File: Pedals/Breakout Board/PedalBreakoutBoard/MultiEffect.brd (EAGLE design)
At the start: 61.9 x 86.3 mm, 69 parts, among them IC1 LD1117V, IC2 MCP6004P, U1 OPA1652AID

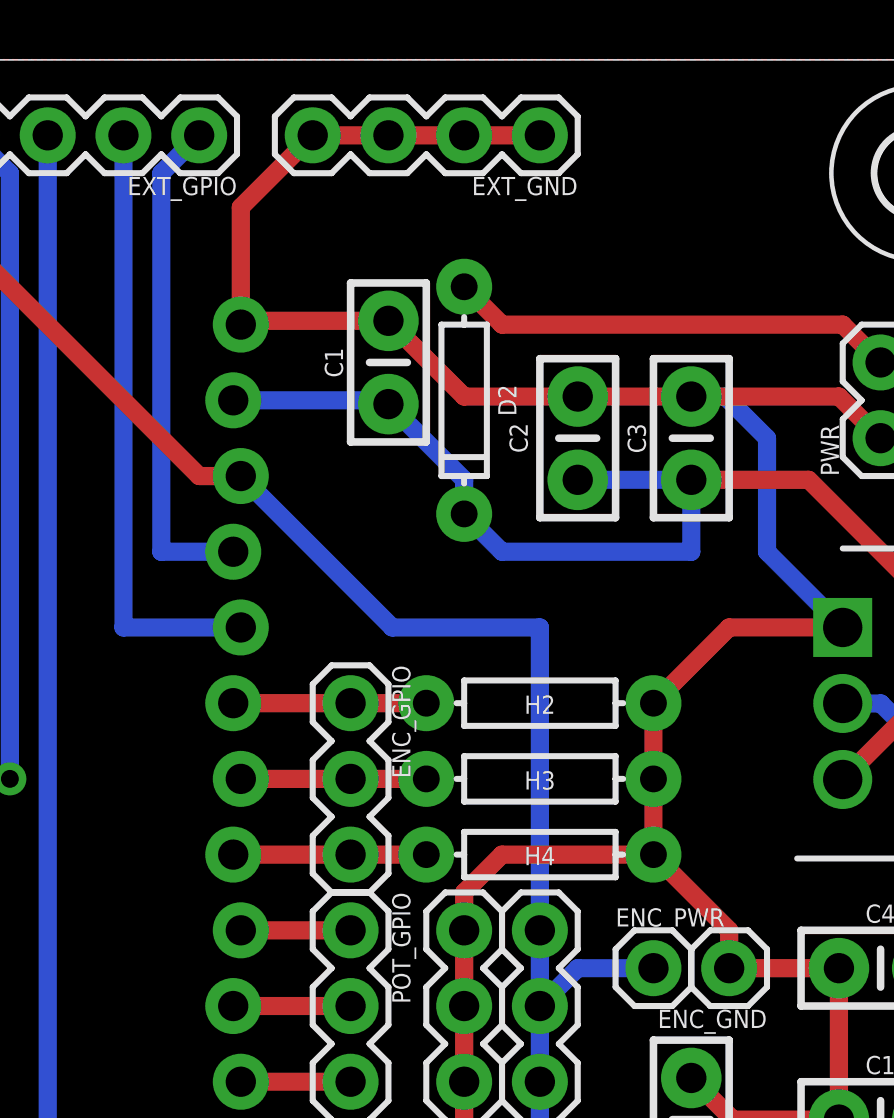
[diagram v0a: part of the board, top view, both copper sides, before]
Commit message: DP-97 - Add power conditioning caps to 3V3_D
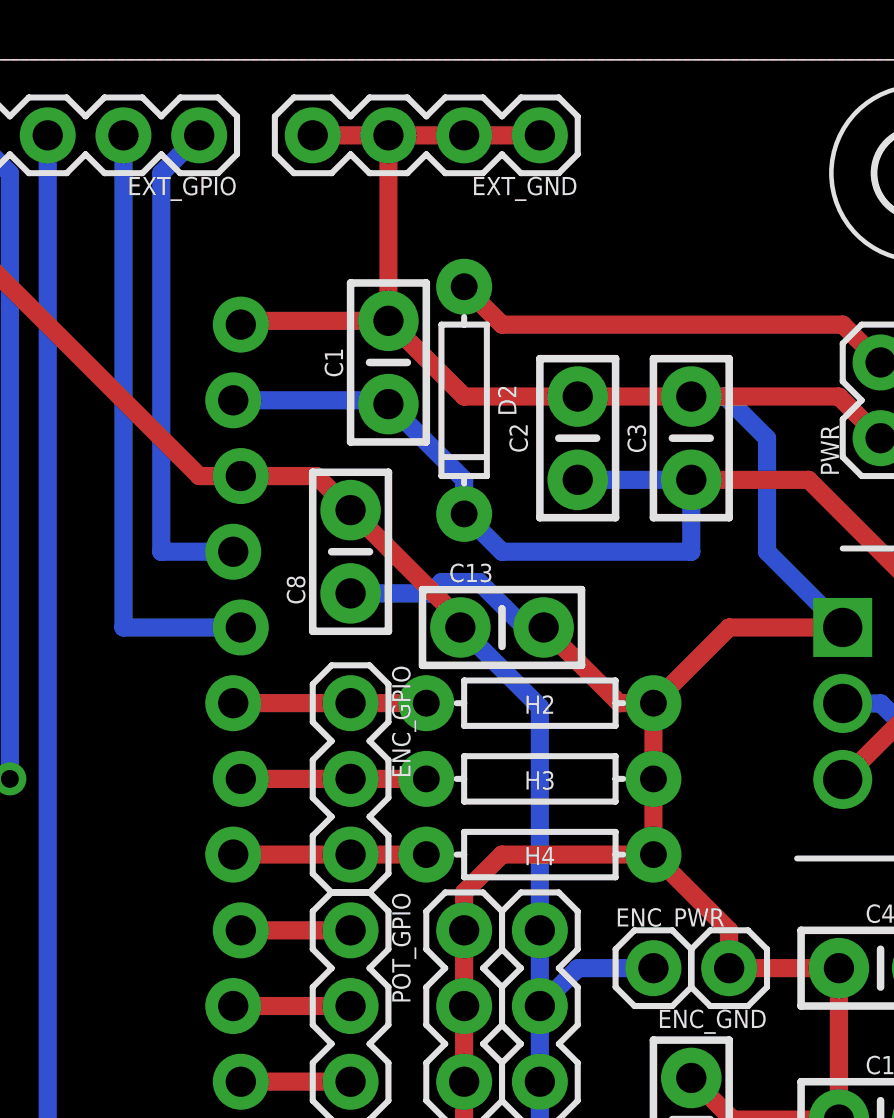
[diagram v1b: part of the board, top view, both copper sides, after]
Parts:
- added C13: 0.1UF, Custom-Parts:CAP-PTH-SMALL-KIT
- added C8: 10UF, Custom-Parts:CAP-PTH-SMALL-KIT
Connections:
- net +3V3_D: now also C13.1, C8.2
- net GND: now also C13.2, C8.1
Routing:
- net GND: track 228.9 -> 239.7 mm
- net +3V3_D: track 132.5 -> 131.1 mm
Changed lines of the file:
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@@
 <attribute name="VALUE" x="17.78" y="85.852" size="0.6096" layer="27" font="vector" ratio="20" rot="R180"/>
+</element>
+<element name="C8" library="Custom-Parts" package="CAP-PTH-SMALL-KIT" value="10UF" x="39.37" y="69.85" smashed="yes" rot="R90">
+<attribute name="NAME" x="37.846" y="68.072" size="0.6096" layer="25" rot="R90"/>
+<attribute name="VALUE" x="41.402" y="68.072" size="0.6096" layer="27" rot="R90"/>
+</element>
+<element name="C13" library="Custom-Parts" package="CAP-PTH-SMALL-KIT" value="0.1UF" x="44.45" y="67.31" smashed="yes">
+<attribute name="NAME" x="42.672" y="68.834" size="0.6096" layer="25"/>
+<attribute name="VALUE" x="42.672" y="65.278" size="0.6096" layer="27"/>
 </element>
 </elements>
 <signals>
 <signal name="GND">
-<contactref element="SEED" pad="40"/>
 <contactref element="PWR" pad="1"/>
 <contactref element="IC1" pad="1"/>
@@
 <contactref element="C1" pad="2"/>
 <wire x1="43.18" y1="75.057" x2="46.99" y2="75.057" width="0.6096" layer="1"/>
-<wire x1="35.687" y1="77.47" x2="35.814" y2="77.597" width="0.6096" layer="1"/>
-<wire x1="35.814" y1="77.597" x2="40.64" y2="77.597" width="0.6096" layer="1"/>
 <wire x1="40.64" y1="77.597" x2="43.18" y2="75.057" width="0.6096" layer="1"/>
 <contactref element="C6" pad="2"/>
@@
 <contactref element="EXT_GND" pad="3"/>
 <contactref element="EXT_GND" pad="4"/>
-<wire x1="35.687" y1="77.47" x2="35.687" y2="81.407" width="0.6096" layer="1"/>
-<wire x1="35.687" y1="81.407" x2="38.1" y2="83.82" width="0.6096" layer="1"/>
 <wire x1="38.1" y1="83.82" x2="40.64" y2="83.82" width="0.6096" layer="1"/>
 <wire x1="40.64" y1="83.82" x2="43.18" y2="83.82" width="0.6096" layer="1"/>
@@
 <wire x1="19.4155" y1="27.94" x2="17.78" y2="27.94" width="0.6096" layer="1"/>
 <wire x1="17.78" y1="27.94" x2="17.78" y2="41.91" width="0.6096" layer="1"/>
+<contactref element="SEED" pad="40"/>
+<contactref element="C8" pad="1"/>
+<contactref element="C13" pad="2"/>
+<wire x1="35.687" y1="77.47" x2="35.814" y2="77.597" width="0.6096" layer="1"/>
+<wire x1="35.814" y1="77.597" x2="40.64" y2="77.597" width="0.6096" layer="1"/>
+<wire x1="40.64" y1="83.82" x2="40.64" y2="77.597" width="0.6096" layer="1"/>
+<wire x1="45.847" y1="67.31" x2="48.387" y2="64.77" width="0.6096" layer="1"/>
+<wire x1="48.387" y1="64.77" x2="49.53" y2="64.77" width="0.6096" layer="1"/>
+<wire x1="43.6842625" y1="68.834" x2="42.4217375" y2="68.834" width="0.6096" layer="16"/>
+<wire x1="45.847" y1="67.31" x2="45.2082625" y2="67.31" width="0.6096" layer="16"/>
+<wire x1="45.2082625" y1="67.31" x2="43.6842625" y2="68.834" width="0.6096" layer="16"/>
+<wire x1="42.4217375" y1="68.834" x2="42.0407375" y2="68.453" width="0.6096" layer="16"/>
+<wire x1="42.0407375" y1="68.453" x2="39.37" y2="68.453" width="0.6096" layer="16"/>
 </signal>
 <signal name="SPST1">
@@
 <wire x1="12.7" y1="57.15" x2="3.81" y2="48.26" width="0.6096" layer="16"/>
 <wire x1="3.81" y1="48.26" x2="3.81" y2="46.99" width="0.6096" layer="16"/>
-<wire x1="35.687" y1="72.39" x2="40.767" y2="67.31" width="0.6096" layer="16"/>
-<wire x1="40.767" y1="67.31" x2="45.72" y2="67.31" width="0.6096" layer="16"/>
-<wire x1="45.72" y1="67.31" x2="45.72" y2="57.15" width="0.6096" layer="16"/>
 <wire x1="45.72" y1="57.15" x2="45.72" y2="54.61" width="0.6096" layer="16"/>
 <wire x1="45.72" y1="54.61" x2="45.72" y2="52.07" width="0.6096" layer="16"/>
@@
 <wire x1="45.72" y1="54.61" x2="46.99" y2="55.88" width="0.6096" layer="16"/>
 <wire x1="46.99" y1="55.88" x2="49.53" y2="55.88" width="0.6096" layer="16"/>
+<contactref element="C8" pad="2"/>
+<contactref element="C13" pad="1"/>
+<wire x1="35.687" y1="72.39" x2="38.227" y2="72.39" width="0.6096" layer="1"/>
+<wire x1="38.227" y1="72.39" x2="39.37" y2="71.247" width="0.6096" layer="1"/>
+<wire x1="39.37" y1="71.247" x2="43.053" y2="67.564" width="0.6096" layer="1"/>
+<wire x1="43.053" y1="67.564" x2="43.053" y2="67.31" width="0.6096" layer="1"/>
+<wire x1="43.053" y1="67.31" x2="45.72" y2="64.643" width="0.6096" layer="16"/>
+<wire x1="45.72" y1="64.643" x2="45.72" y2="57.15" width="0.6096" layer="16"/>
 </signal>
 <signal name="SCL">
